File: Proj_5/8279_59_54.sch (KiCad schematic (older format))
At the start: 43 parts, among them J4 Conn_02x07_Counter_Clockwise, J5 Conn_02x04_Top_Bottom, SW10 Switch_SW_SPST, SW11 Switch_SW_SPST, SW12 Switch_SW_SPST, SW13 Switch_SW_SPST, SW14 Switch_SW_SPST, SW15 Switch_SW_SPST, SW16 Switch_SW_SPST, SW17 Switch_SW_SPST, SW18 Switch_SW_SPST, SW19 Switch_SW_SPST, SW2 Shift, SW20 Switch_SW_SPST, SW21 Switch_SW_SPST, SW22 Switch_SW_SPST, SW23 Switch_SW_SPST, SW24 NMI Button, SW25 Reset Button, SW26 IR0 Button, SW3 Switch_SW_SPST, SW4 Switch_SW_SPST, SW5 Switch_SW_SPST, SW6 Switch_SW_SPST, SW7 CTRL, SW8 Switch_SW_SPST, SW9 Switch_SW_SPST, U10 8259, U11 8254, U17 pkd8279, U18 74LS138, U35 PAL16L8, U38 PAL16L8, U48 MAX6816, U49 MAX6816, U50 MAX6816

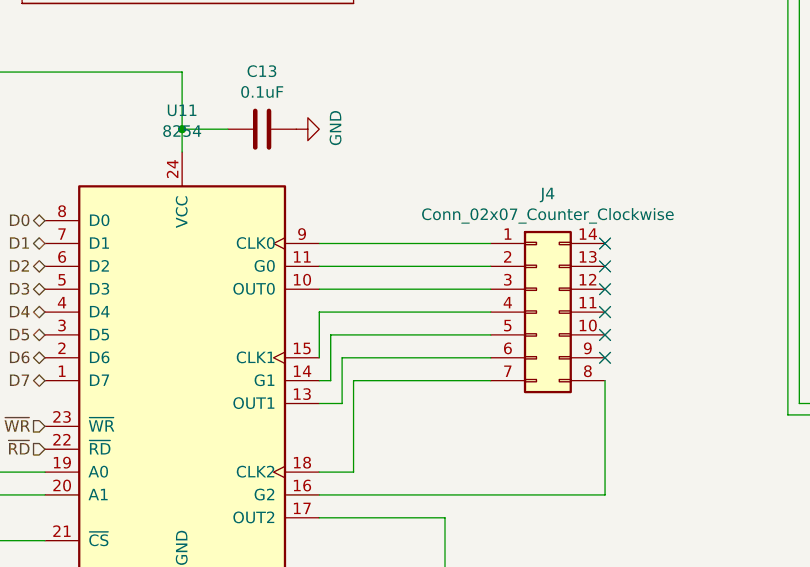
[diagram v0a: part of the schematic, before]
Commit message: More Headers - 690 to 540 No-Connects
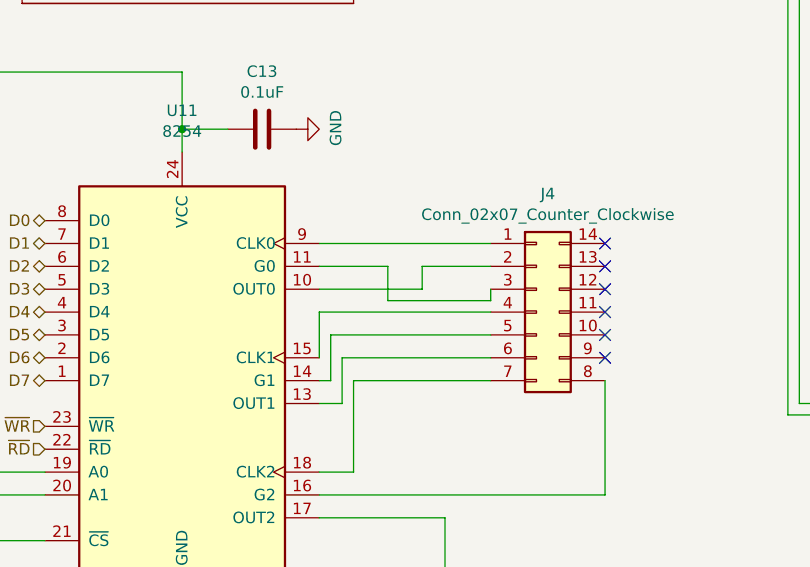
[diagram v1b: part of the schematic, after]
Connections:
- net at U11.10 (OUT0): now also J4.2 (Pin_2); no longer J4.3 (Pin_3)
- net at U11.11 (G0): now also J4.3 (Pin_3); no longer J4.2 (Pin_2)
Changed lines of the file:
@@
 	7150 6900 7900 6900
-Wire Wire Line
-	7150 7000 7900 7000
-Wire Wire Line
-	7150 7100 7900 7100
 Wire Wire Line
 	7150 7400 7150 7200
@@
 	1850 1450 2100 1450
 Connection ~ 1850 1450
+Wire Wire Line
+	7150 7000 7450 7000
+Wire Wire Line
+	7450 7000 7450 7150
+Wire Wire Line
+	7450 7150 7900 7150
+Wire Wire Line
+	7900 7150 7900 7100
+Wire Wire Line
+	7150 7100 7600 7100
+Wire Wire Line
+	7600 7100 7600 7000
+Wire Wire Line
+	7600 7000 7900 7000
 $EndSCHEMATC
